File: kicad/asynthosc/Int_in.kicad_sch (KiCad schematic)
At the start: 6 parts, among them J5 AudioJack2, Q2 Q_NPN_BEC, SW3 TRG0

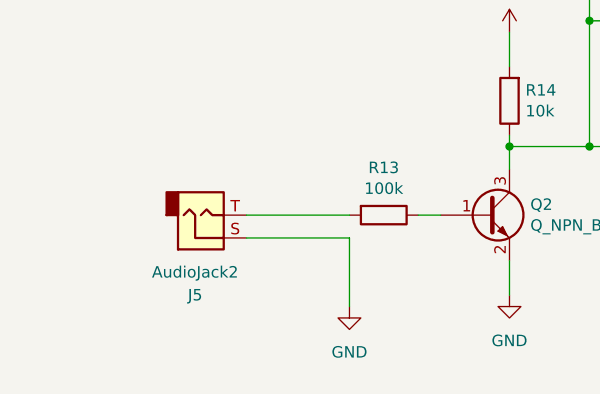
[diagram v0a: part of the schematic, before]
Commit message: sch: add spi nor, display connection, and more footprints
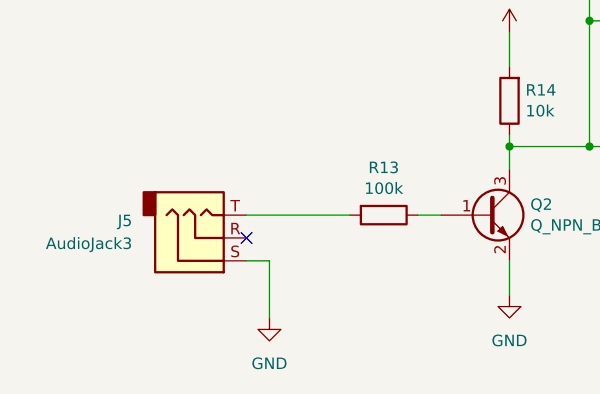
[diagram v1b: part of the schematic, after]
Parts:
- removed J5: AudioJack2, symbol Connector_Audio:AudioJack2
- added J5: AudioJack3, symbol Connector_Audio:AudioJack3
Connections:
- net GND: now also J5.S
- net at R13.2: now also J5.T
- no-connect marks 0 -> 1
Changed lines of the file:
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@@
 		(color 0 0 0 0)
 	)
+	(no_connect
+		(at 55.88 68.58)
+	)
 	(wire
 		(pts
@@
 	(wire
 		(pts
-			(xy 55.88 68.58) (xy 67.31 68.58)
-		)
-		(stroke
-			(width 0)
-			(type default)
-		)
-	)
-	(wire
-		(pts
 			(xy 100.33 44.45) (xy 93.98 44.45)
 		)
@@
 	(wire
 		(pts
+			(xy 58.42 71.12) (xy 58.42 77.47)
+		)
+		(stroke
+			(width 0)
+			(type default)
+		)
+	)
+	(wire
+		(pts
 			(xy 67.31 66.04) (xy 55.88 66.04)
 		)
@@
 	(wire
 		(pts
-			(xy 67.31 68.58) (xy 67.31 76.2)
-		)
-		(stroke
-			(width 0)
-			(type default)
-		)
-	)
-	(wire
-		(pts
 			(xy 109.22 58.42) (xy 116.84 58.42)
 		)
@@
 		(pts
 			(xy 85.09 58.42) (xy 93.98 58.42)
+		)
+		(stroke
+			(width 0)
+			(type default)
+		)
+	)
+	(wire
+		(pts
+			(xy 58.42 71.12) (xy 55.88 71.12)
 		)
 		(stroke
@@
 			)
 			(justify left)
+		)
+	)
+	(symbol
+		(lib_id "power:GND")
+		(at 58.42 77.47 0)
+		(unit 1)
+		(exclude_from_sim no)
+		(in_bom yes)
+		(on_board yes)
+		(dnp no)
+		(fields_autoplaced yes)
+		(property "Reference" "#PWR092"
+			(at 58.42 83.82 0)
+			(effects
+				(font
+					(size 1.27 1.27)
+				)
+				(hide yes)
+			)
+		)
+		(property "Value" "GND"
+			(at 58.42 82.55 0)
+			(effects
+				(font
+					(size 1.27 1.27)
+				)
+			)
+		)
+		(property "Footprint" ""
+			(at 58.42 77.47 0)
+			(effects
+				(font
+					(size 1.27 1.27)
+				)
+				(hide yes)
+			)
+		)
+		(property "Datasheet" ""
+			(at 58.42 77.47 0)
+			(effects
+				(font
+					(size 1.27 1.27)
+				)
+				(hide yes)
+			)
+		)
+		(property "Description" "Power symbol creates a global label with name \"GND\" , ground"
+			(at 58.42 77.47 0)
+			(effects
+				(font
+					(size 1.27 1.27)
+				)
+				(hide yes)
+			)
+		)
+		(pin "1"
+		)
+		(instances
+			(project "asynthosc"
+				(path "/d73e377a-a016-415f-8824-91cc6e4907b9/5f8430bb-1923-4d76-b418-f207310879ec/1b493739-e50b-4e48-bad0-48b50a96f04e"
+					(reference "#PWR092")
+					(unit 1)
+				)
+			)
+		)
+	)
+	(symbol
+		(lib_id "Connector_Audio:AudioJack3")
+		(at 50.8 68.58 0)
+		(mirror x)
+		(unit 1)
+		(exclude_from_sim no)
+		(in_bom yes)
+		(on_board yes)
+		(dnp no)
+		(property "Reference" "J5"
+			(at 43.18 66.6749 0)
+			(effects
+				(font
+					(size 1.27 1.27)
+				)
+				(justify right)
+			)
+		)
+		(property "Value" "AudioJack3"
+			(at 43.18 69.2149 0)
+			(effects
+				(font
+					(size 1.27 1.27)
+				)
+				(justify right)
+			)
+		)
+		(property "Footprint" ""
+			(at 50.8 68.58 0)
+			(effects
+				(font
+					(size 1.27 1.27)
+				)
+				(hide yes)
+			)
+		)
+		(property "Datasheet" "~"
+			(at 50.8 68.58 0)
+			(effects
+				(font
+					(size 1.27 1.27)
+				)
+				(hide yes)
+			)
+		)
+		(property "Description" "Audio Jack, 3 Poles (Stereo / TRS)"
+			(at 50.8 68.58 0)
+			(effects
+				(font
+					(size 1.27 1.27)
+				)
+				(hide yes)
+			)
+		)
+		(property "Sim.Device" "V"
+			(at 50.8 68.58 0)
+			(effects
+				(font
+					(size 1.27 1.27)
+				)
+				(hide yes)
+			)
+		)
+		(property "Sim.Type" "PULSE"
+			(at 50.8 68.58 0)
+			(effects
+				(font
+					(size 1.27 1.27)
+				)
+				(hide yes)
+			)
+		)
+		(property "Sim.Pins" "S=- T=+"
+			(at 50.8 68.58 0)
+			(effects
+				(font
+					(size 1.27 1.27)
+				)
+				(hide yes)
+			)
+		)
+		(property "Sim.Params" "y1=0 y2=12 td=0 tr=0 tf=0 tw=0.1 per=1"
+			(at 50.8 68.58 0)
+			(effects
+				(font
+					(size 1.27 1.27)
+				)
+				(hide yes)
+			)
+		)
+		(pin "S"
+		)
+		(pin "R"
+		)
+		(pin "T"
+		)
+		(instances
+			(project "asynthosc"
+				(path "/d73e377a-a016-415f-8824-91cc6e4907b9/5f8430bb-1923-4d76-b418-f207310879ec/1b493739-e50b-4e48-bad0-48b50a96f04e"
+					(reference "J5")
+					(unit 1)
+				)
+			)
 		)
 	)
@@
 	)
 	(symbol
-		(lib_id "power:GND")
-		(at 67.31 76.2 0)
-		(unit 1)
-		(exclude_from_sim no)
-		(in_bom yes)
-		(on_board yes)
-		(dnp no)
-		(fields_autoplaced yes)
-		(property "Reference" "#PWR029"
-			(at 67.31 82.55 0)
-			(effects
-				(font
-					(size 1.27 1.27)
-				)
-				(hide yes)
-			)
-		)
-		(property "Value" "GND"
-			(at 67.31 81.28 0)
-			(effects
-				(font
-					(size 1.27 1.27)
-				)
-			)
-		)
-		(property "Footprint" ""
-			(at 67.31 76.2 0)
-			(effects
-				(font
-					(size 1.27 1.27)
-				)
-				(hide yes)
-			)
-		)
-		(property "Datasheet" ""
-			(at 67.31 76.2 0)
-			(effects
-				(font
-					(size 1.27 1.27)
-				)
-				(hide yes)
-			)
-		)
-		(property "Description" "Power symbol creates a global label with name \"GND\" , ground"
-			(at 67.31 76.2 0)
-			(effects
-				(font
-					(size 1.27 1.27)
-				)
-				(hide yes)
-			)
-		)
-		(pin "1"
-		)
-		(instances
-			(project "asynthosc"
-				(path "/d73e377a-a016-415f-8824-91cc6e4907b9/5f8430bb-1923-4d76-b418-f207310879ec/1b493739-e50b-4e48-bad0-48b50a96f04e"
-					(reference "#PWR029")
-					(unit 1)
-				)
-			)
-		)
-	)
-	(symbol
 		(lib_id "power:+3V3")
 		(at 85.09 45.72 0)
@@
 					(unit 1)
 				)
-			)
-		)
-	)
-	(symbol
-		(lib_id "Connector_Audio:AudioJack2")
-		(at 50.8 66.04 0)
-		(mirror x)
-		(unit 1)
-		(exclude_from_sim no)
-		(in_bom yes)
-		(on_board yes)
-		(dnp no)
-		(property "Reference" "J5"
-			(at 50.165 74.93 0)
-			(effects
-				(font
-					(size 1.27 1.27)
-				)
-			)
-		)
-		(property "Value" "AudioJack2"
-			(at 50.165 72.39 0)
-			(effects
-				(font
-					(size 1.27 1.27)
-				)
-			)
-		)
-		(property "Footprint" ""
-			(at 50.8 66.04 0)
-			(effects
-				(font
-					(size 1.27 1.27)
-				)
-				(hide yes)
-			)
-		)
-		(property "Datasheet" "~"
-			(at 50.8 66.04 0)
-			(effects
-				(font
-					(size 1.27 1.27)
-				)
-				(hide yes)
-			)
-		)
-		(property "Description" "Audio Jack, 2 Poles (Mono / TS)"
-			(at 50.8 66.04 0)
-			(effects
-				(font
-					(size 1.27 1.27)
-				)
-				(hide yes)
-			)
-		)
-		(property "Sim.Device" "V"
-			(at 50.8 66.04 0)
-			(effects
-				(font
-					(size 1.27 1.27)
-				)
-				(hide yes)
-			)
-		)
-		(property "Sim.Type" "PULSE"
-			(at 50.8 66.04 0)
-			(effects
-				(font
-					(size 1.27 1.27)
-				)
-				(hide yes)
-			)
-		)
-		(property "Sim.Pins" "S=- T=+"
-			(at 50.8 66.04 0)
-			(effects
-				(font
-					(size 1.27 1.27)
-				)
-				(hide yes)
-			)
-		)
-		(property "Sim.Params" "y1=0 y2=12 td=1 tr=0.005 tf=0.005 tw=0.1 per=1"
-			(at 50.8 66.04 0)
-			(effects
-				(font
-					(size 1.27 1.27)
-				)
-				(hide yes)
-			)
-		)
-		(pin "S"
-		)
-		(pin "T"
-		)
-		(instances
-			(project "asynthosc"
-				(path "/d73e377a-a016-415f-8824-91cc6e4907b9/5f8430bb-1923-4d76-b418-f207310879ec/1b493739-e50b-4e48-bad0-48b50a96f04e"
-					(reference "J5")
-					(unit 1)
-				)

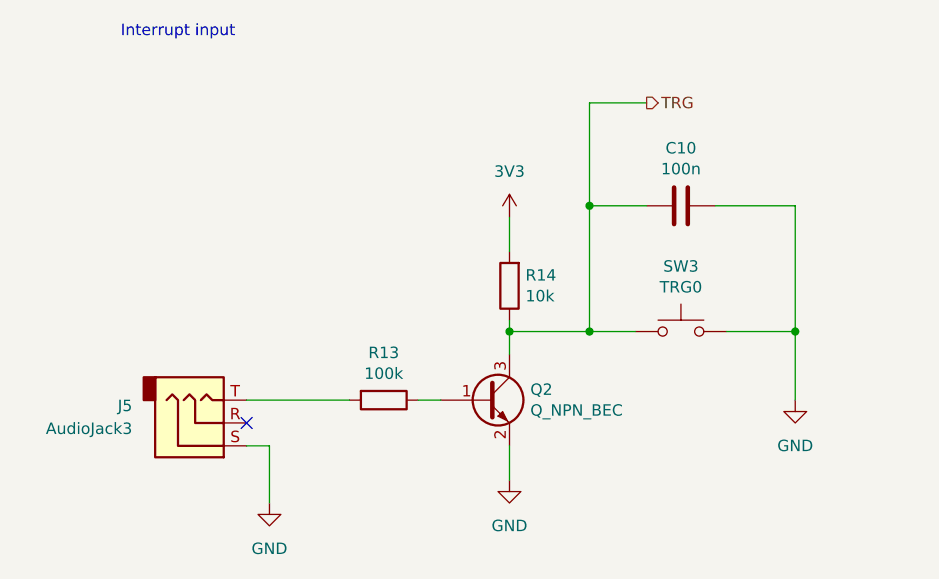
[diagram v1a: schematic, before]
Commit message: sch: update footprint links
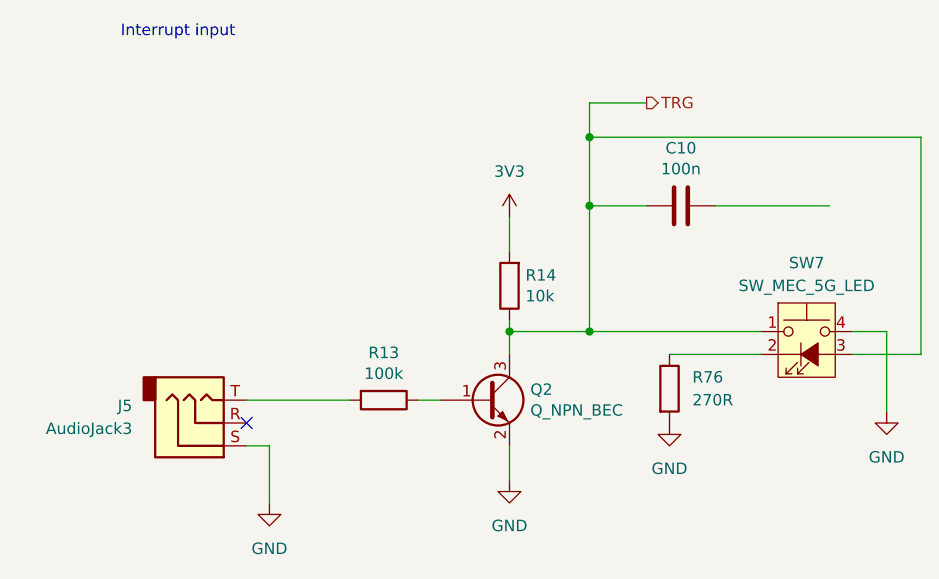
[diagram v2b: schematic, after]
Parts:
- removed SW3: TRG0, switches:SW_6425, symbol Switch:SW_Push
- added R76: 270R, Resistor_SMD:R_0402_1005Metric, symbol Device:R
- added SW7: SW_MEC_5G_LED, asynthosc:TPB01-X0XLXX_SW_MEC_5G, symbol Switch:SW_MEC_5G_LED
- J5: footprint (none) -> asynthosc:Jack_3.5mm_3legs_XKB_PJ-3411_Vertical
- Q2: footprint Package_TO_SOT_SMD:SOT-23 -> (none)
- R13, R14: footprint Resistor_SMD:R_0603_1608Metric -> Resistor_SMD:R_0402_1005Metric
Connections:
- net GND: now also R76.2, SW7.4 (A); no longer C10.1
- net TRG: now also SW7.1, SW7.3 (K)
- new net: R76.1, SW7.2

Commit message: wip
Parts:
- Q1: renamed from Q2; footprint (none) -> Package_TO_SOT_SMD:SOT-23; RefNum (none) -> JSMSEMI S8050-J3Y
- renumbered C10 to C57, J5 to J8, R13 to R80, R14 to R81, R76 to R82, SW7 to SW10
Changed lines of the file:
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@@
 		(dnp no)
 		(fields_autoplaced yes)
-		(property "Reference" "#PWR092"
+		(property "Reference" "#PWR0137"
 			(at 58.42 83.82 0)
 			(effects
@@
 		(instances
 			(project "asynthosc"
+				(path "/d73e377a-a016-415f-8824-91cc6e4907b9/5f8430bb-1923-4d76-b418-f207310879ec/00719137-6b38-42a6-b28f-e4711c0869df"
+					(reference "#PWR0137")
+					(unit 1)
+				)
 				(path "/d73e377a-a016-415f-8824-91cc6e4907b9/5f8430bb-1923-4d76-b418-f207310879ec/1b493739-e50b-4e48-bad0-48b50a96f04e"
 					(reference "#PWR092")
@@
 		(dnp no)
 		(fields_autoplaced yes)
-		(property "Reference" "#PWR0132"
+		(property "Reference" "#PWR0140"
 			(at 102.87 74.93 0)
 			(effects
@@
 		(instances
 			(project "asynthosc"
+				(path "/d73e377a-a016-415f-8824-91cc6e4907b9/5f8430bb-1923-4d76-b418-f207310879ec/00719137-6b38-42a6-b28f-e4711c0869df"
+					(reference "#PWR0140")
+					(unit 1)
+				)
 				(path "/d73e377a-a016-415f-8824-91cc6e4907b9/5f8430bb-1923-4d76-b418-f207310879ec/1b493739-e50b-4e48-bad0-48b50a96f04e"
 					(reference "#PWR0132")
@@
 		(dnp no)
 		(fields_autoplaced yes)
-		(property "Reference" "SW7"
+		(property "Reference" "SW10"
 			(at 118.11 50.8 0)
 			(effects
@@
 		(instances
 			(project "asynthosc"
+				(path "/d73e377a-a016-415f-8824-91cc6e4907b9/5f8430bb-1923-4d76-b418-f207310879ec/00719137-6b38-42a6-b28f-e4711c0869df"
+					(reference "SW10")
+					(unit 1)
+				)
 				(path "/d73e377a-a016-415f-8824-91cc6e4907b9/5f8430bb-1923-4d76-b418-f207310879ec/1b493739-e50b-4e48-bad0-48b50a96f04e"
 					(reference "SW7")
@@
 		(on_board yes)
 		(dnp no)
-		(property "Reference" "J5"
+		(property "Reference" "J8"
 			(at 43.18 66.6749 0)
 			(effects
@@
 		(instances
 			(project "asynthosc"
+				(path "/d73e377a-a016-415f-8824-91cc6e4907b9/5f8430bb-1923-4d76-b418-f207310879ec/00719137-6b38-42a6-b28f-e4711c0869df"
+					(reference "J8")
+					(unit 1)
+				)
 				(path "/d73e377a-a016-415f-8824-91cc6e4907b9/5f8430bb-1923-4d76-b418-f207310879ec/1b493739-e50b-4e48-bad0-48b50a96f04e"
 					(reference "J5")
@@
 		(on_board yes)
 		(dnp no)
-		(property "Reference" "R13"
+		(property "Reference" "R80"
 			(at 71.12 60.7822 90)
 			(effects
@@
 		(instances
 			(project "asynthosc"
+				(path "/d73e377a-a016-415f-8824-91cc6e4907b9/5f8430bb-1923-4d76-b418-f207310879ec/00719137-6b38-42a6-b28f-e4711c0869df"
+					(reference "R80")
+					(unit 1)
+				)
 				(path "/d73e377a-a016-415f-8824-91cc6e4907b9/5f8430bb-1923-4d76-b418-f207310879ec/1b493739-e50b-4e48-bad0-48b50a96f04e"
 					(reference "R13")
@@
 		(dnp no)
 		(fields_autoplaced yes)
-		(property "Reference" "#PWR031"
+		(property "Reference" "#PWR0139"
 			(at 85.09 81.28 0)
 			(effects
@@
 		(instances
 			(project "asynthosc"
+				(path "/d73e377a-a016-415f-8824-91cc6e4907b9/5f8430bb-1923-4d76-b418-f207310879ec/00719137-6b38-42a6-b28f-e4711c0869df"
+					(reference "#PWR0139")
+					(unit 1)
+				)
 				(path "/d73e377a-a016-415f-8824-91cc6e4907b9/5f8430bb-1923-4d76-b418-f207310879ec/1b493739-e50b-4e48-bad0-48b50a96f04e"
 					(reference "#PWR031")
@@
 		(dnp no)
 		(fields_autoplaced yes)
-		(property "Reference" "#PWR030"
+		(property "Reference" "#PWR0138"
 			(at 85.09 49.53 0)
 			(effects
@@
 		(instances
 			(project "asynthosc"
+				(path "/d73e377a-a016-415f-8824-91cc6e4907b9/5f8430bb-1923-4d76-b418-f207310879ec/00719137-6b38-42a6-b28f-e4711c0869df"
+					(reference "#PWR0138")
+					(unit 1)
+				)
 				(path "/d73e377a-a016-415f-8824-91cc6e4907b9/5f8430bb-1923-4d76-b418-f207310879ec/1b493739-e50b-4e48-bad0-48b50a96f04e"
 					(reference "#PWR030")
@@
 		(dnp no)
 		(fields_autoplaced yes)
-		(property "Reference" "R76"
+		(property "Reference" "R82"
 			(at 105.41 63.4999 0)
 			(effects
@@
 		(instances
 			(project "asynthosc"
+				(path "/d73e377a-a016-415f-8824-91cc6e4907b9/5f8430bb-1923-4d76-b418-f207310879ec/00719137-6b38-42a6-b28f-e4711c0869df"
+					(reference "R82")
+					(unit 1)
+				)
 				(path "/d73e377a-a016-415f-8824-91cc6e4907b9/5f8430bb-1923-4d76-b418-f207310879ec/1b493739-e50b-4e48-bad0-48b50a96f04e"
 					(reference "R76")
@@
 		(dnp no)
 		(fields_autoplaced yes)
-		(property "Reference" "#PWR0130"
+		(property "Reference" "#PWR0141"
 			(at 127 73.66 0)
 			(effects
@@
 		(instances
 			(project "asynthosc"
+				(path "/d73e377a-a016-415f-8824-91cc6e4907b9/5f8430bb-1923-4d76-b418-f207310879ec/00719137-6b38-42a6-b28f-e4711c0869df"
+					(reference "#PWR0141")
+					(unit 1)
+				)
 				(path "/d73e377a-a016-415f-8824-91cc6e4907b9/5f8430bb-1923-4d76-b418-f207310879ec/1b493739-e50b-4e48-bad0-48b50a96f04e"
 					(reference "#PWR0130")
@@
 		(on_board yes)
 		(dnp no)
-		(property "Reference" "C10"
+		(property "Reference" "C57"
 			(at 104.14 38.0492 90)
 			(effects
@@
 		(instances
 			(project "asynthosc"
+				(path "/d73e377a-a016-415f-8824-91cc6e4907b9/5f8430bb-1923-4d76-b418-f207310879ec/00719137-6b38-42a6-b28f-e4711c0869df"
+					(reference "C57")
+					(unit 1)
+				)
 				(path "/d73e377a-a016-415f-8824-91cc6e4907b9/5f8430bb-1923-4d76-b418-f207310879ec/1b493739-e50b-4e48-bad0-48b50a96f04e"
 					(reference "C10")
@@
 		(on_board yes)
 		(dnp no)
-		(property "Reference" "Q2"
+		(property "Reference" "Q1"
 			(at 87.4014 64.8716 0)
 			(effects
@@
 			)
 		)
-		(property "Footprint" ""
+		(property "Footprint" "Package_TO_SOT_SMD:SOT-23"
 			(at 87.63 63.5 0)
 			(effects
@@
 			)
 		)
+		(property "RefNum" "JSMSEMI S8050-J3Y"
+			(at 82.55 66.04 0)
+			(effects
+				(font
+					(size 1.27 1.27)
+				)
+				(hide yes)
+			)
+		)
 		(pin "1"
 		)
@@
 		(instances
 			(project "asynthosc"
+				(path "/d73e377a-a016-415f-8824-91cc6e4907b9/5f8430bb-1923-4d76-b418-f207310879ec/00719137-6b38-42a6-b28f-e4711c0869df"
+					(reference "Q1")
+					(unit 1)
+				)
 				(path "/d73e377a-a016-415f-8824-91cc6e4907b9/5f8430bb-1923-4d76-b418-f207310879ec/1b493739-e50b-4e48-bad0-48b50a96f04e"
 					(reference "Q2")
@@
 		(on_board yes)
 		(dnp no)
-		(property "Reference" "R14"
+		(property "Reference" "R81"
 			(at 86.868 52.1716 0)
 			(effects
@@
 		(instances
 			(project "asynthosc"
+				(path "/d73e377a-a016-415f-8824-91cc6e4907b9/5f8430bb-1923-4d76-b418-f207310879ec/00719137-6b38-42a6-b28f-e4711c0869df"
+					(reference "R81")
+					(unit 1)
+				)
 				(path "/d73e377a-a016-415f-8824-91cc6e4907b9/5f8430bb-1923-4d76-b418-f207310879ec/1b493739-e50b-4e48-bad0-48b50a96f04e"
 					(reference "R14")

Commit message: sch: change stm32 for smaller one, create smaller jumper footprint
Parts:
- C57: RefNum (none) -> _generic_
- J8: Manufacturer (none) -> XKB; RefNum (none) -> PJ-3411
- Q1: Manufacturer (none) -> JSMSEMI; RefNum JSMSEMI S8050-J3Y -> S8050-J3Y
- SW10: Manufacturer (none) -> ROCPU; RefNum (none) -> TPB01-3016L6W
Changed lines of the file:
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@@
+			)
+		)
+		(property "LCSC" ""
+			(at 118.11 60.96 0)
+			(effects
+				(font
+					(size 1.27 1.27)
+				)
+				(hide yes)
+			)
+		)
+		(property "Manufacturer" "ROCPU"
+			(at 118.11 60.96 0)
+			(effects
+				(font
+					(size 1.27 1.27)
+				)
+				(hide yes)
+			)
+		)
+		(property "RefNum" "TPB01-3016L6W"
+			(at 118.11 60.96 0)
+			(effects
+				(font
+					(size 1.27 1.27)
+				)
+				(hide yes)
 			)
 		)
@@
 			)
 		)
+		(property "LCSC" ""
+			(at 50.8 68.58 0)
+			(effects
+				(font
+					(size 1.27 1.27)
+				)
+				(hide yes)
+			)
+		)
+		(property "Manufacturer" "XKB"
+			(at 50.8 68.58 0)
+			(effects
+				(font
+					(size 1.27 1.27)
+				)
+				(hide yes)
+			)
+		)
+		(property "RefNum" "PJ-3411 "
+			(at 50.8 68.58 0)
+			(effects
+				(font
+					(size 1.27 1.27)
+				)
+				(hide yes)
+			)
+		)
 		(pin "S"
 		)
@@
 		)
 		(property "Description" ""
+			(at 71.12 66.04 0)
+			(effects
+				(font
+					(size 1.27 1.27)
+				)
+				(hide yes)
+			)
+		)
+		(property "LCSC" ""
+			(at 71.12 66.04 0)
+			(effects
+				(font
+					(size 1.27 1.27)
+				)
+				(hide yes)
+			)
+		)
+		(property "Manufacturer" ""
 			(at 71.12 66.04 0)
 			(effects
@@
 			)
 		)
+		(property "LCSC" ""
+			(at 102.87 64.77 0)
+			(effects
+				(font
+					(size 1.27 1.27)
+				)
+				(hide yes)
+			)
+		)
+		(property "Manufacturer" ""
+			(at 102.87 64.77 0)
+			(effects
+				(font
+					(size 1.27 1.27)
+				)
+				(hide yes)
+			)
+		)
 		(pin "1"
 		)
@@
 			)
 		)
+		(property "LCSC" ""
+			(at 104.14 44.45 0)
+			(effects
+				(font
+					(size 1.27 1.27)
+				)
+				(hide yes)
+			)
+		)
+		(property "Manufacturer" ""
+			(at 104.14 44.45 0)
+			(effects
+				(font
+					(size 1.27 1.27)
+				)
+				(hide yes)
+			)
+		)
+		(property "RefNum" "_generic_"
+			(at 104.14 44.45 0)
+			(effects
+				(font
+					(size 1.27 1.27)
+				)
+				(hide yes)
+			)
+		)
 		(pin "2"
 		)
@@
 			)
 		)
-		(property "RefNum" "JSMSEMI S8050-J3Y"
+		(property "RefNum" " S8050-J3Y"
+			(at 82.55 66.04 0)
+			(effects
+				(font
+					(size 1.27 1.27)
+				)
+				(hide yes)
+			)
+		)
+		(property "LCSC" ""
+			(at 82.55 66.04 0)
+			(effects
+				(font
+					(size 1.27 1.27)
+				)
+				(hide yes)
+			)
+		)
+		(property "Manufacturer" "JSMSEMI"
 			(at 82.55 66.04 0)
 			(effects
@@
 			(at 85.09 53.34 0)
 			(effects
+				(font
+					(size 1.27 1.27)
+				)
+				(hide yes)
+			)
+		)
+		(property "LCSC" ""
+			(at 85.09 53.34 0)
+			(effects
+				(font
+					(size 1.27 1.27)
+				)
+				(hide yes)
+			)
+		)
+		(property "Manufacturer" ""
+			(at 85.09 53.34 0)
+			(effects
